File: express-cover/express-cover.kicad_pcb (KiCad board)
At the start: 2 copper layers, 180 x 35 mm, 26 parts

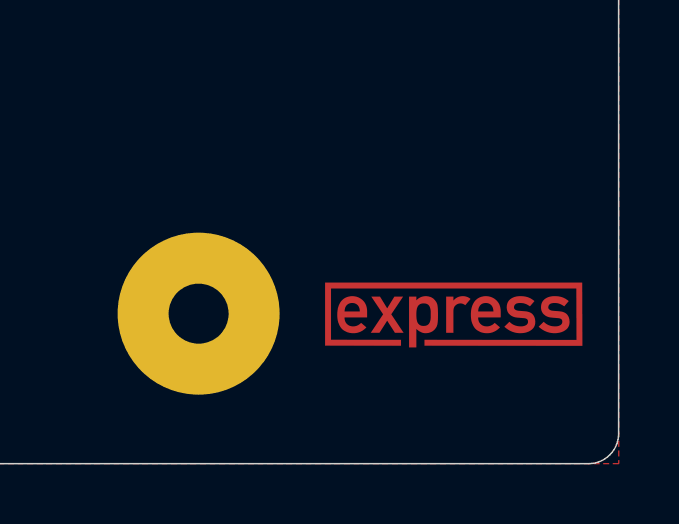
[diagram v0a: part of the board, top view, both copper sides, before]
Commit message: Use the correct TRS pins
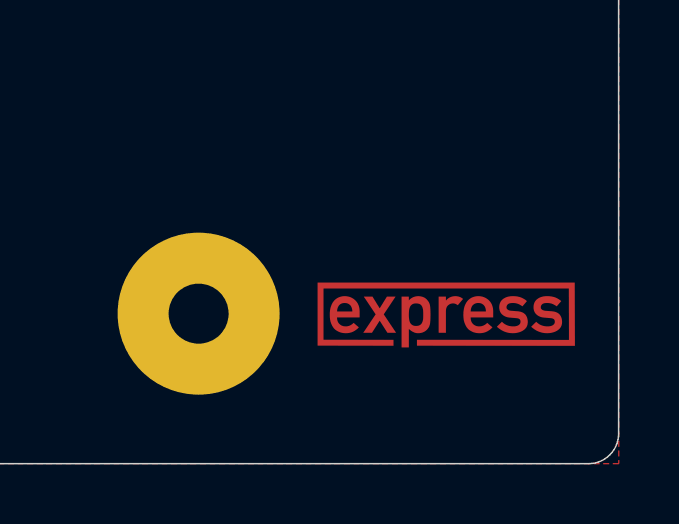
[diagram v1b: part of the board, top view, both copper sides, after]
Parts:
- moved ICON101 0.25 mm to (291.2, 110.0)
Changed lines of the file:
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@@
 		)
 	)
-	(property "Order-Number" "ORDER-NUMBER")
+	(property "Order-Number" "JLCJLCJLCJLC")
 	(net 0 "")
 	(net 1 "GND")
@@
 	(footprint "V2_Artwork:Board_express_Small"
 		(layer "F.Cu")
-		(at 291.5 110)
+		(at 291.25 110)
 		(property "Reference" "ICON101"
 			(at 0 -3 0)
@@
 			(polygon
 				(pts
-					(xy 295.902788 111.179279) (xy 287.110623 111.179278) (xy 287.110623 108.851875) (xy 295.902788 108.851876)
+					(xy 295.652788 111.179279) (xy 286.860623 111.179278) (xy 286.860623 108.851875) (xy 295.652788 108.851876)
 				)
 			)
 		)
 		(group ""
-			(members "0346be3f-eb06-4f2a-95ff-da1bc17b16a9" "0a2727fd-d977-46f2-9043-9bfbe6a535ca"
-				"3b279b40-83e6-40ac-b28c-0192e85402e6" "5b1cb084-9835-4c84-9e77-d218c2c45b16"
-				"7c84bff9-5ab0-450e-97f9-6f2b4b208222" "e3e40e23-0b66-4ea4-910f-e9b9eca13818"
-				"ee2c415d-e9e0-43fe-a494-7e33bef9e1ad" "fce30dec-8015-4fc3-9762-0c341a0f5c7f"
+			(members "227a5c6a-a04f-4145-becf-07c3895e7261" "4aee5faa-ecb6-451f-a01d-cce12aaf376d"
+				"6222f6a8-2289-4c43-9d72-a04bdab1f56a" "9deea049-e8bc-47ba-b01e-249d1a88c799"
+				"a2f9ed4f-5fc4-481e-9b77-84858102a9dd" "a43a5561-0fdf-4c7a-8c15-0827d0debfa9"
+				"e77e9a5e-1cc0-4e4d-9469-81fa56af0442" "e9fee349-6c0b-43cf-bc96-1a4120c7c2fc"
 			)
 		)
 		(group ""
-			(members "026211f4-d79a-49c5-9c7b-a863da5c766d" "1124ad8e-257e-44b6-a5f9-52aa92d3f875"
-				"5a50c1ff-acea-4192-80a8-0f1827eb50b3" "6cc682f2-dfa2-4db0-8628-0d0b199c966e"
-				"8db577de-1c8d-46c1-accd-872874df45d1" "958a682a-66ee-4f4e-b513-da96eb2c13ad"
-				"d5298d22-189b-4ca3-b58a-33f347c94028" "ff1e5287-1f31-45f3-9125-ae97134d6531"
+			(members "1c0fff37-9094-46ee-8b05-56441ef3157a" "20f348ff-5ad2-44aa-a40a-a967a9c0c8a8"
+				"4e608cac-c6de-4dbb-bbe2-1b0843bef2b8" "69a26cd5-1132-43ef-8b7e-15309358cf07"
+				"853664fd-8019-4114-a221-b27adab56c39" "d3ec8b9a-eaa5-4be8-9c8c-a7fb6c990fb3"
+				"e05f56cf-6c97-4169-8b30-17fdc2be63f8" "ece61aaa-2dfd-45eb-a0dd-31e7d3ba5b72"
 			)
 		)
